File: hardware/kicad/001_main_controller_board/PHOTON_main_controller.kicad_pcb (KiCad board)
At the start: 2 copper layers, 69 x 49.9 mm, 94 parts, among them J1 FH34SRJ-18S-0.5SH(50), J102 JST_SH RS-485_1, J103 JST_SH RS-485_2, J3 USB_C_Receptacle_USB2.0, J4 Micro_SD_Card, J6 Conn_01x04, Q106 WM02N08F, SW1 SW_Push, U1 RP2350_60QFN, U101 APS6404L-3SQR-ZR, U102 THVD1424RGTR, U108 VCNT2025X01, U2 NCP1117-3.3_SOT223, U3 W25Q128JVPIQ, U4 TPD4E05U06DQAR, Y1 ABM8-272-T3

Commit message: Consolidate footprints into a single shared library
All three boards carried their own copies of the same footprints - 79
files across 11 project libraries for 37 distinct footprints. Several
existed three times over (RP2350-QFN-60 ThermalVias, edge_holes,
TO-236_VIS-L, SON_NT2020_VIS, L_pol_2016, USB_Micro-B). Three copies
drift, and this project has already been bitten twice by a library and
a board disagreeing.

- New hardware/kicad/common.pretty holds all 37, verified byte-identical
  where they were duplicated: zero name collisions with differing
  content, so nothing had to be reconciled.
- Each board's fp-lib-table is now a single "common" entry. Previously
  001 alone had eight, and the nickname "footprints" meant a different
  library on each of the three boards - so lib_ids were rewritten per
  board, not globally.
- 459 footprint references across the three boards now resolve. That
  includes SparkFun-Qwiic:qwiic_8mm on 001, which was referenced but
  had never been in any fp-lib-table - broken before this change.

Also shrinks docs/images/reflective_sensor.png from 2816x1536 / 4.43 MB
to 1600x873 / 1.72 MB.

Co-Authored-By: Claude Opus 5 <noreply@anthropic.com>
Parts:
- C2, C3: footprint RP2350_60QFN_minimal:C_0402_1005Metric_small_pads -> common:C_0402_1005Metric_small_pads
- G***: footprint SparkFun-Qwiic:qwiic_8mm -> common:qwiic_8mm
- J1: footprint Pretty Custom:CONN18x1_FH34SRJ-18S-0.5SH50_HIR -> common:CONN18x1_FH34SRJ-18S-0.5SH50_HIR
- J4: footprint Pretty Custom:TF-015_corrected -> common:TF-015_corrected
- L1: footprint RP2350_60QFN_minimal:L_pol_2016 -> common:L_pol_2016
- Q106: footprint footprints:WM02N08F -> common:WM02N08F
- U1: footprint RP2350_60QFN_minimal:RP2350-QFN-60-1EP_7x7_P0.4mm_EP3.4x3.4mm_ThermalVias -> common:RP2350-QFN-60-1EP_7x7_P0.4mm_EP3.4x3.4mm_ThermalVias
- U101: footprint Pretty Custom:PSON50P200X300X50-9N -> common:PSON50P200X300X50-9N
- U102: footprint Pretty Custom:QFN_24RGTR_TEX -> common:QFN_24RGTR_TEX
- U108: footprint footprints:VCNT2025X01_VIS -> common:VCNT2025X01_VIS
- U3: footprint small_flash:WSON_128JVPIQ_WIN -> common:WSON_128JVPIQ_WIN
- U4: footprint Pretty Custom:DQA0010A -> common:DQA0010A
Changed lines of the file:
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@@
 		)
 	)
-	(footprint "footprints:VCNT2025X01_VIS"
+	(footprint "common:VCNT2025X01_VIS"
 		(layer "F.Cu")
 		(at 14.63 2.94)
@@
 		)
 	)
-	(footprint "Pretty Custom:TF-015_corrected"
+	(footprint "common:TF-015_corrected"
 		(layer "F.Cu")
 		(at 50.65 4.235 180)
@@
 		)
 	)
-	(footprint "Pretty Custom:CONN18x1_FH34SRJ-18S-0.5SH50_HIR"
+	(footprint "common:CONN18x1_FH34SRJ-18S-0.5SH50_HIR"
 		(layer "F.Cu")
 		(at 54.9651 24.944493 -90)
@@
 		)
 	)
-	(footprint "RP2350_60QFN_minimal:RP2350-QFN-60-1EP_7x7_P0.4mm_EP3.4x3.4mm_ThermalVias"
+	(footprint "common:RP2350-QFN-60-1EP_7x7_P0.4mm_EP3.4x3.4mm_ThermalVias"
 		(layer "F.Cu")
 		(at 34.765 25.97 180)
@@
 		)
 	)
-	(footprint "small_flash:WSON_128JVPIQ_WIN"
+	(footprint "common:WSON_128JVPIQ_WIN"
 		(layer "F.Cu")
 		(at 42 34.2522 -90)
@@
 		(embedded_fonts no)
 	)
-	(footprint "Pretty Custom:PSON50P200X300X50-9N"
+	(footprint "common:PSON50P200X300X50-9N"
 		(layer "F.Cu")
 		(at 43.66 40.44 180)
@@
 		)
 	)
-	(footprint "Pretty Custom:DQA0010A"
+	(footprint "common:DQA0010A"
 		(layer "F.Cu")
 		(at 34.349998 38.925 -90)
@@
 		)
 	)
-	(footprint "RP2350_60QFN_minimal:C_0402_1005Metric_small_pads"
+	(footprint "common:C_0402_1005Metric_small_pads"
 		(layer "F.Cu")
 		(at 32.695 30.61 180)
@@
 		)
 	)
-	(footprint "SparkFun-Qwiic:qwiic_8mm"
+	(footprint "common:qwiic_8mm"
 		(layer "F.Cu")
 		(at 33.5 9.08 180)
@@
 		)
 	)
-	(footprint "RP2350_60QFN_minimal:C_0402_1005Metric_small_pads"
+	(footprint "common:C_0402_1005Metric_small_pads"
 		(layer "F.Cu")
 		(at 32.695 31.59 180)
@@
 		)
 	)
-	(footprint "Pretty Custom:QFN_24RGTR_TEX"
+	(footprint "common:QFN_24RGTR_TEX"
 		(layer "F.Cu")
 		(at 59.398389 38.613352 -90)
@@
 		)
 	)
-	(footprint "footprints:WM02N08F"
+	(footprint "common:WM02N08F"
 		(layer "F.Cu")
 		(at 17.09 3.605)
@@
 		)
 	)
-	(footprint "RP2350_60QFN_minimal:L_pol_2016"
+	(footprint "common:L_pol_2016"
 		(layer "F.Cu")
 		(at 32.38 33.16 180)

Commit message: Rename shared footprint library common -> photon_common
'common' is too generic for a library nickname - it can collide with a
global library or another project's table, and it doesn't identify whose
footprints these are.

155 lib_ids rewritten across the three boards plus all three
fp-lib-tables. All 459 footprint references still resolve.

Co-Authored-By: Claude Opus 5 <noreply@anthropic.com>
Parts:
- C2, C3: footprint common:C_0402_1005Metric_small_pads -> photon_common:C_0402_1005Metric_small_pads
- G***: footprint common:qwiic_8mm -> photon_common:qwiic_8mm
- J1: footprint common:CONN18x1_FH34SRJ-18S-0.5SH50_HIR -> photon_common:CONN18x1_FH34SRJ-18S-0.5SH50_HIR
- J4: footprint common:TF-015_corrected -> photon_common:TF-015_corrected
- L1: footprint common:L_pol_2016 -> photon_common:L_pol_2016
- Q106: footprint common:WM02N08F -> photon_common:WM02N08F
- U1: footprint common:RP2350-QFN-60-1EP_7x7_P0.4mm_EP3.4x3.4mm_ThermalVias -> photon_common:RP2350-QFN-60-1EP_7x7_P0.4mm_EP3.4x3.4mm_ThermalVias
- U101: footprint common:PSON50P200X300X50-9N -> photon_common:PSON50P200X300X50-9N
- U102: footprint common:QFN_24RGTR_TEX -> photon_common:QFN_24RGTR_TEX
- U108: footprint common:VCNT2025X01_VIS -> photon_common:VCNT2025X01_VIS
- U3: footprint common:WSON_128JVPIQ_WIN -> photon_common:WSON_128JVPIQ_WIN
- U4: footprint common:DQA0010A -> photon_common:DQA0010A
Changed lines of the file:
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@@
 		)
 	)
-	(footprint "common:VCNT2025X01_VIS"
+	(footprint "photon_common:VCNT2025X01_VIS"
 		(layer "F.Cu")
 		(at 14.63 2.94)
@@
 		)
 	)
-	(footprint "common:TF-015_corrected"
+	(footprint "photon_common:TF-015_corrected"
 		(layer "F.Cu")
 		(at 50.65 4.235 180)
@@
 		)
 	)
-	(footprint "common:CONN18x1_FH34SRJ-18S-0.5SH50_HIR"
+	(footprint "photon_common:CONN18x1_FH34SRJ-18S-0.5SH50_HIR"
 		(layer "F.Cu")
 		(at 54.9651 24.944493 -90)
@@
 		)
 	)
-	(footprint "common:RP2350-QFN-60-1EP_7x7_P0.4mm_EP3.4x3.4mm_ThermalVias"
+	(footprint "photon_common:RP2350-QFN-60-1EP_7x7_P0.4mm_EP3.4x3.4mm_ThermalVias"
 		(layer "F.Cu")
 		(at 34.765 25.97 180)
@@
 		)
 	)
-	(footprint "common:WSON_128JVPIQ_WIN"
+	(footprint "photon_common:WSON_128JVPIQ_WIN"
 		(layer "F.Cu")
 		(at 42 34.2522 -90)
@@
 		(embedded_fonts no)
 	)
-	(footprint "common:PSON50P200X300X50-9N"
+	(footprint "photon_common:PSON50P200X300X50-9N"
 		(layer "F.Cu")
 		(at 43.66 40.44 180)
@@
 		)
 	)
-	(footprint "common:DQA0010A"
+	(footprint "photon_common:DQA0010A"
 		(layer "F.Cu")
 		(at 34.349998 38.925 -90)
@@
 		)
 	)
-	(footprint "common:C_0402_1005Metric_small_pads"
+	(footprint "photon_common:C_0402_1005Metric_small_pads"
 		(layer "F.Cu")
 		(at 32.695 30.61 180)
@@
 		)
 	)
-	(footprint "common:qwiic_8mm"
+	(footprint "photon_common:qwiic_8mm"
 		(layer "F.Cu")
 		(at 33.5 9.08 180)
@@
 		)
 	)
-	(footprint "common:C_0402_1005Metric_small_pads"
+	(footprint "photon_common:C_0402_1005Metric_small_pads"
 		(layer "F.Cu")
 		(at 32.695 31.59 180)
@@
 		)
 	)
-	(footprint "common:QFN_24RGTR_TEX"
+	(footprint "photon_common:QFN_24RGTR_TEX"
 		(layer "F.Cu")
 		(at 59.398389 38.613352 -90)
@@
 		)
 	)
-	(footprint "common:WM02N08F"
+	(footprint "photon_common:WM02N08F"
 		(layer "F.Cu")
 		(at 17.09 3.605)
@@
 		)
 	)
-	(footprint "common:L_pol_2016"
+	(footprint "photon_common:L_pol_2016"
 		(layer "F.Cu")
 		(at 32.38 33.16 180)

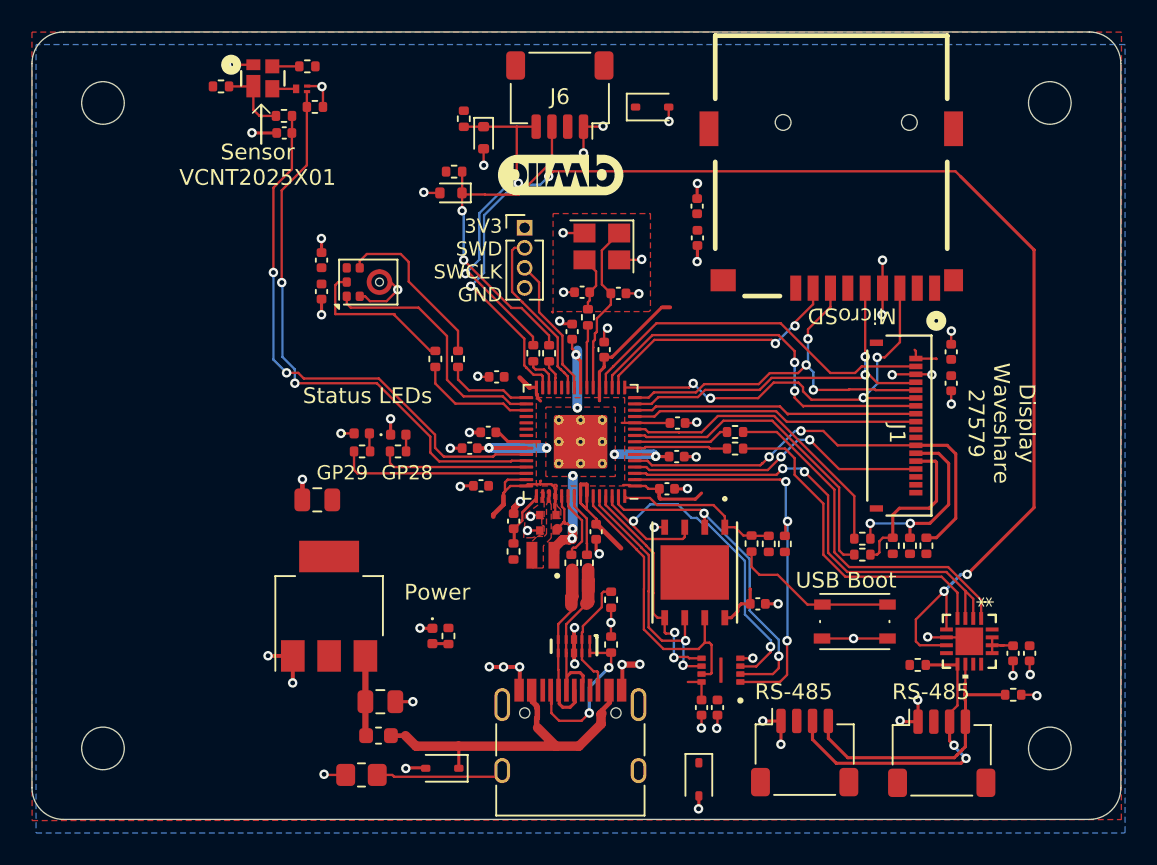
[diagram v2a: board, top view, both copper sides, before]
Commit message: Consolidate symbol libraries, normalise BOM data, Rev B for all three boards
Libraries
- Move PHOTON and PHOTON_Modified to hardware/kicad/, shared by all three
  projects, replacing six divergent per-project copies. 002's versions taken
  as canonical (correct pin electrical types); 001-only parts recovered from
  the schematic cache. All 459 footprint and 464 symbol refs resolve.
- Repoint every sym-lib-table at the shared files. Nicknames unchanged, so
  002 and 001d needed no lib_id edits; only 001's stale date-named ones.
- Fix stale footprint nicknames inside the symbol libraries (footprints:,
  RP2350_60QFN_minimal:, APS6404L-3SQR-ZR:) that would have made newly
  placed parts land with unresolvable footprints.
- Reset baked-in reference designators and MPNs on six library footprints
  back to REF** and the footprint name. SOT-563_DRL0006A carried "U6",
  which would have overwritten 001d's U5 on any field-resetting update.

Footprints
- Add SON-8_3x2mm_P0.5mm: KiCad stock SON-8 with the exposed pad and its
  four paste apertures removed. The APS6404L USON-8L (JEDEC MO-229) has no
  thermal pad and 0-0.05mm standoff, so both the copper and the paste under
  the body were wrong. Replaces the easyeda2kicad footprint on U101, whose
  0.102mm mask margin also bridged all six 0.5mm-pitch mask openings.
- Mounting holes on 001 and 001d move to the photon_common keepout
  footprint, matching 002, so a screw head cannot bridge the F.Cu power
  pour to the B.Cu ground pour.
- Remove the unused TDK T3902 microphone footprint.

BOM
- Normalise values fleet-wide: Greek mu -> ascii u, strip spaces before
  units, complete truncated inductor values. Each was splitting one part
  into two BOM lines, since the fab toolkit groups on footprint+value.
- Unify JST-SH connector values so each board emits one line, not three.
  Per-connector labels moved to Description, which is not a BOM column.
- Assign part numbers to the four largest passive lines: 100nF C1525,
  1uF C52923, 1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
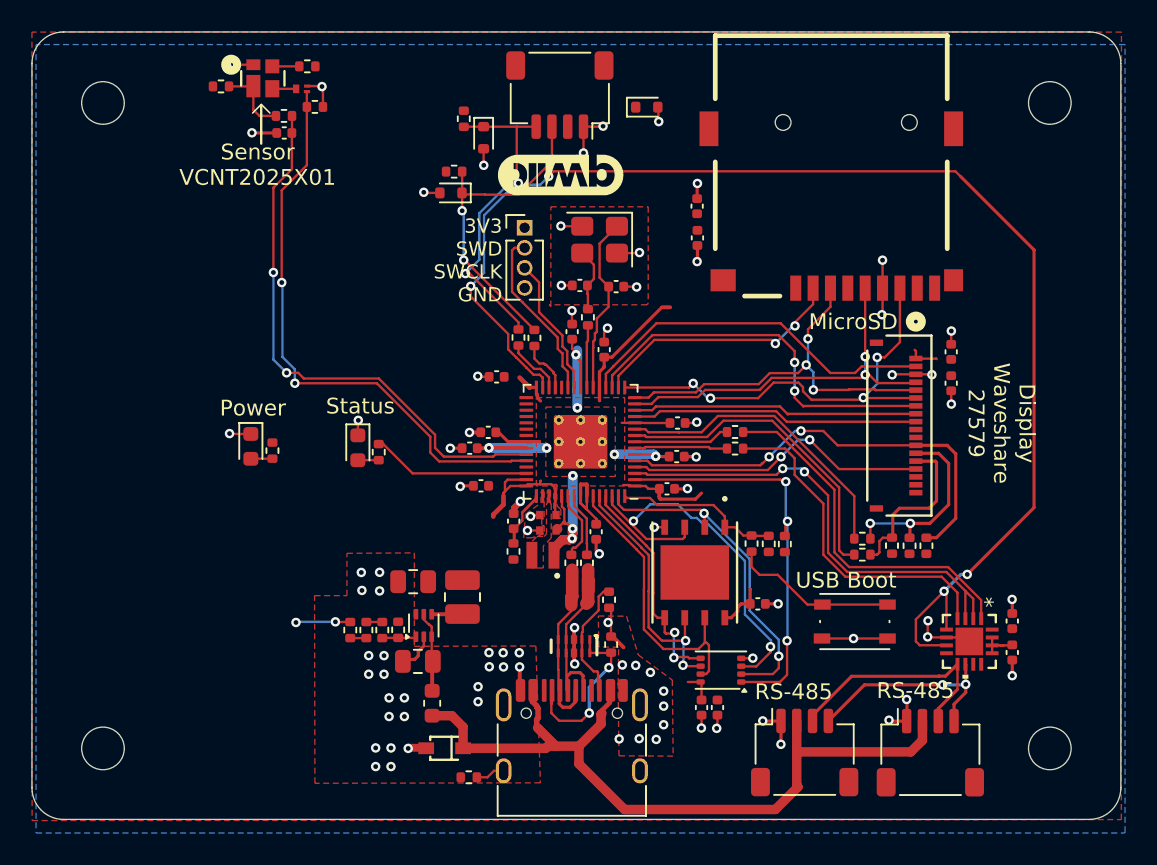
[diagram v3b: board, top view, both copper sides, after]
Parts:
- removed C103: 100nF, Capacitor_SMD:C_0402_1005Metric
- removed C104: 1μF, Capacitor_SMD:C_0402_1005Metric
- removed CR101, CR5: H7VHD3UA, Diode_SMD:D_SOD-323
- removed D1: LED GREEN, LED_SMD:LED_0402_1005Metric
- removed MK1: SPH0645LM4H, Sensor_Audio:Knowles_SPH0645LM4H-6_3.5x2.65mm
- removed R107: 430Ω, Resistor_SMD:R_0402_1005Metric
- removed U102: THVD1424RGTR, photon_common:QFN_24RGTR_TEX
- removed U2: NCP1117-3.3_SOT223, Package_TO_SOT_SMD:SOT-223-3_TabPin2
- added D12: D_TVS, Diode_SMD:D_SOD-523, F.Cu at (39.0, 4.76)
- added L2: 1uH, Inductor_SMD:L_1008_2520Metric, F.Cu at (27.3, 35.8)
- added U5: THVD1424RGTR, photon_common:QFN_24RGTR_TEX, F.Cu at (59.4, 38.6)
- added U6: TPS62A0569ADRLR, photon_common:SOT-563_DRL0006A, F.Cu at (24.8, 37.6)
- C1: value 10uF -> 4.7uF
- C10: value 100nF -> 1uF
- C102, C106, C108: value 1μF -> 1uF
- C4: value 10uF -> 22uF
- C9: value 220pF -> 100nF
- CR1: value H7VHD3UA -> PTVSHC3D7VU; footprint Diode_SMD:D_SOD-323 -> photon_common:SOD-323_L1.8-W1.3-LS2.5-RD
- D2: footprint LED_SMD:LED_0402_1005Metric -> LED_SMD:LED_0603_1608Metric
- D3: value LED GREEN -> LED RED; footprint LED_SMD:LED_0402_1005Metric -> LED_SMD:LED_0603_1608Metric
- H101, H102, H103, H104: footprint MountingHole:MountingHole_2.7mm_M2.5_ISO7380 -> photon_common:MountingHole_2.7mm_M2.5_Keepout
- J102: value JST_SH RS-485_1 -> JST_SH
- J103: value JST_SH RS-485_2 -> JST_SH
- J6: value Conn_01x04 -> JST_SH
- L1: value 3.3u -> 3.3uH
- R1: value 1MΩ -> 0Ω; footprint Resistor_SMD:R_0805_2012Metric_Pad1.20x1.40mm_HandSolder -> Resistor_SMD:R_0402_1005Metric
- R10, R119, R121: value 10 kΩ -> 10kΩ
- R103: value 4.7kΩ -> 100kΩ
- R104: value 4.7kΩ -> 200kΩ
- R105: value 100kΩ -> 200kΩ
- R106: value 430Ω -> 51kΩ
- R120: value 68 Ω -> 68Ω
- R13: value 49.9Ω -> 4.7kΩ
- R2, R3: value 5.1 kΩ -> 5.1kΩ
- R4: value 10kΩ -> 100kΩ
- R5: value 22kΩ -> 10kΩ
- R9: value 22Ω -> 4.7kΩ
- U101: footprint photon_common:PSON50P200X300X50-9N -> photon_common:SON-8_3x2mm_P0.5mm
- moved C10 49.4 mm to (62.1, 39.3)
- moved C9 49.4 mm to (62.1, 37.3)
- moved R104 35.9 mm to (20.2, 37.9), turned to 90 degrees
- moved R106 34.0 mm to (22.2, 37.9), turned to 90 degrees
- moved R103 31.8 mm to (23.2, 37.9), turned to 90 degrees
- moved R9 31.3 mm to (54.5, 32.5), turned to -90 degrees
- moved R13 31.0 mm to (55.6, 32.6)
- moved R105 27.1 mm to (21.2, 37.9), turned to -90 degrees
- moved R4 25.2 mm to (47.7, 32.5), turned to 90 degrees
- moved D3 16.6 mm to (13.9, 26.3)
- moved R8 16.2 mm to (15.2, 26.5)
- moved C4 7.99 mm to (24.2, 34.8)
- moved R1 6.80 mm to (27.7, 47.2)
- moved FB1 3.97 mm to (25.4, 42.5), turned to 90 degrees
- moved C1 3.49 mm to (24.5, 39.9), turned to 180 degrees
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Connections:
- CR1 pad 1: VBUS -> +5V
- FB1 pad 1: VBUS -> +5V
- J102 pad 2: +3V3 -> +5V
- J103 pad 2: +3V3 -> +5V
- J3 pad A4: VBUS -> +5V
- J3 pad A9: VBUS -> +5V
- J3 pad B4: VBUS -> +5V
- J3 pad B9: VBUS -> +5V
- R103 pad 1: /I2C_1_SDA -> Net-(U6-FB)
- R103 pad 2: +3V3 -> GND
- R104 pad 1: /I2C_1_SCL -> Net-(R104-Pad1)
- R105 pad 1: +3V3 -> Net-(R105-Pad1)
- R105 pad 2: /GPIO0 -> Net-(R104-Pad1)
- R106 pad 1: /RS485_P -> Net-(U6-FB)
- R106 pad 2: +3V3 -> Net-(R105-Pad1)
- R13 pad 1: /I2S_BCLK -> /I2C_1_SCL
- R13 pad 2: /GPIO19 -> +3V3
- R4 pad 1: Net-(D1-A) -> +3V3
- R4 pad 2: /GPIO28_ADC2 -> /GPIO0
- R9 pad 1: /GPIO21 -> /I2C_1_SDA
- R9 pad 2: Net-(MK1-DATA) -> +3V3
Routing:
- net +5V: track 0.00 -> 50.1 mm
- net VBUS: track 22.2 -> 0.00 mm
- net /GPIO20: track 16.1 -> 0.00 mm
- net GND: track 83.0 -> 67.5 mm, vias 68 -> 86
- net /I2S_BCLK: track 10.9 -> 0.00 mm
- net Net-(MK1-DATA): track 9.99 -> 0.00 mm
- net /GPIO28_ADC2: track 9.48 -> 0.00 mm
- net /GPIO21: track 7.52 -> 0.00 mm
- net /RS485_N: track 20.9 -> 13.6 mm, vias 0 -> 2
- net Net-(J3-SHIELD): track 8.13 -> 1.87 mm
- net /GPIO19: track 5.59 -> 0.00 mm
- net /RS485_P: track 20.3 -> 15.0 mm, vias 2 -> 0
- net Net-(U6-FB): track 0.00 -> 2.16 mm
- net /GPIO29_ADC3: track 12.2 -> 10.1 mm
- net Net-(U6-SW): track 0.00 -> 1.96 mm
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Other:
- board text added: "Noah Jaffe PHOTON RP2350 MCU Board A001 REV B"
- board text added: "Status"
- board text removed: "GP28"
- board text removed: "GP29"
- board text removed: "Noah Jaffe PHOTON RP2350 MCU Board A003 REV C"
- board text removed: "Status LEDs"
